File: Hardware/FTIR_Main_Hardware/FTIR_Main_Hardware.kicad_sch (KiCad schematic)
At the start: 62 parts, among them J1 RJ45_LED_Shielded, Q1 IRF7606PBF, Q2 BSS138, Q3 IRF7606PBF, Q4 IRF7606PBF, Q5 BSS138, Q6 BSS138, U1 MCP6L01x-xOT, U3 OKI, U5 MCP6L01x-xOT, U6 Teensy4.1_DEV-16771, U7 OKI

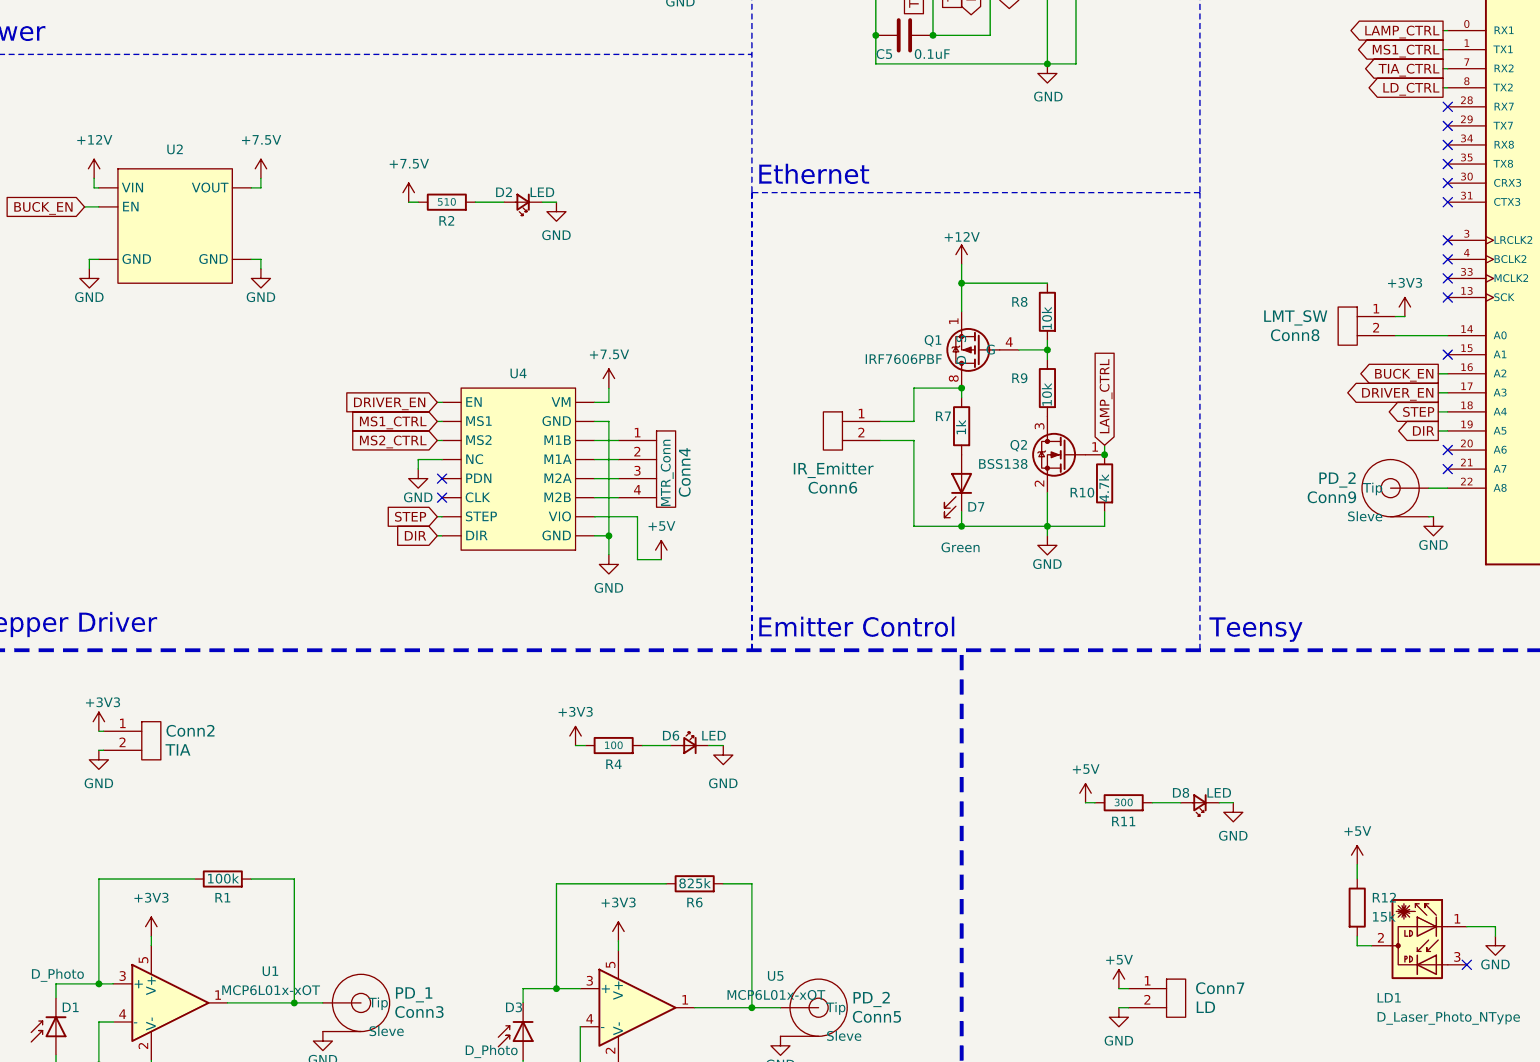
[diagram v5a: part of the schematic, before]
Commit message: Footprint assignments
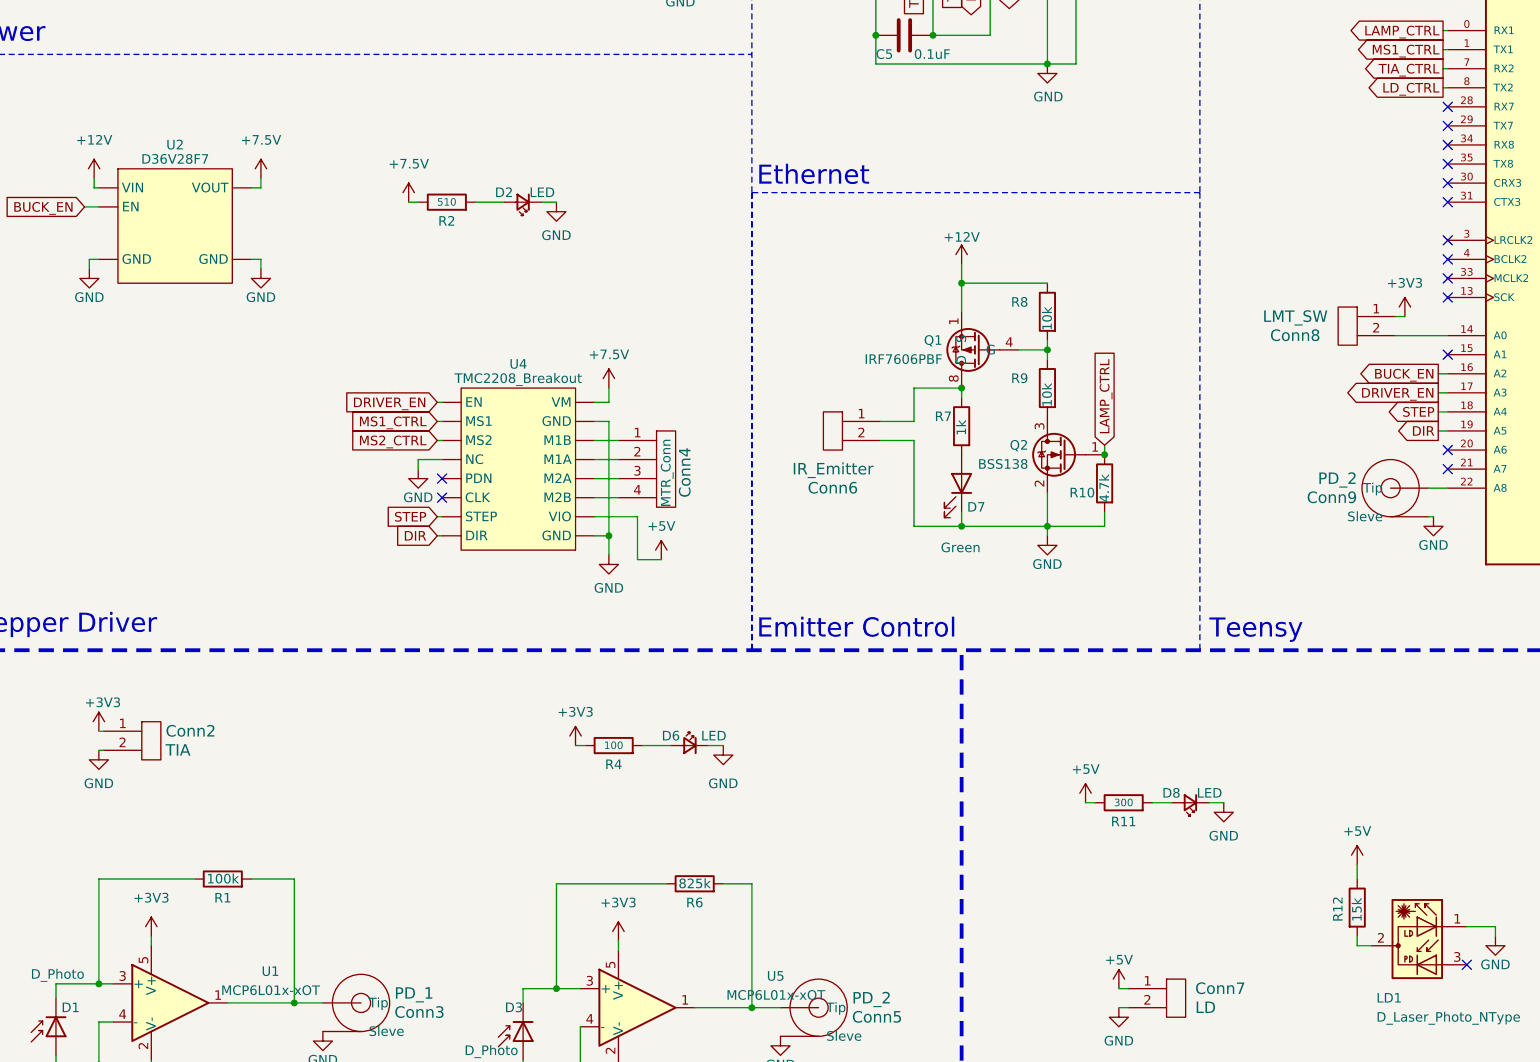
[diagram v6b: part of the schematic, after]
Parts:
- Conn1: footprint (none) -> MRDT_Connectors:Anderson_2_Horizontal_Stacked
- Conn11, Conn12, Conn2, Conn6, Conn7, Conn8: footprint (none) -> MRDT_Connectors:MOLEX_SL_02_Vertical
- Conn4: footprint (none) -> MRDT_Connectors:MOLEX_SL_04_Vertical
- R1, R12, R6: footprint (none) -> LED_SMD:LED_0603_1608Metric_Pad1.05x0.95mm_HandSolder
- U2: value ~ -> D36V28F7
- U3, U7: footprint (none) -> MRDT_Devices:OKI_Horizontal
- U4: value ~ -> TMC2208_Breakout
- U6: footprint MODULE_DEV-16771 -> MRDT_Shields:Teensy_4_1
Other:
- moved on the sheet: D8
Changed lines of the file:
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@@
     (stroke (width 0) (type default))
   )
-  (wire (pts (xy 179.705 154.305) (xy 181.61 154.305))
+  (wire (pts (xy 178.435 154.305) (xy 180.34 154.305))
     (stroke (width 0) (type default))
   )
@@
     (stroke (width 0) (type default))
   )
-  (wire (pts (xy 170.815 154.305) (xy 174.625 154.305))
+  (wire (pts (xy 170.815 154.305) (xy 173.355 154.305))
     (stroke (width 0) (type default))
   )
@@
     )
   )
-  (symbol (lib_id "Device:LED_Small") (at 177.165 154.305 180) (unit 1)
+  (symbol (lib_id "Device:LED_Small") (at 175.895 154.305 180) (unit 1)
     (in_bom yes) (on_board yes) (dnp no)
-    (property "Reference" "D8" (at 174.625 153.035 0)
+    (property "Reference" "D8" (at 173.355 153.035 0)
       (effects (font (size 1.27 1.27)))
     )
-    (property "Value" "LED" (at 179.705 153.035 0)
+    (property "Value" "LED" (at 178.435 153.035 0)
       (effects (font (size 1.27 1.27)))
     )
-    (property "Footprint" "LED_SMD:LED_0603_1608Metric_Pad1.05x0.95mm_HandSolder" (at 177.165 154.305 90)
+    (property "Footprint" "LED_SMD:LED_0603_1608Metric_Pad1.05x0.95mm_HandSolder" (at 175.895 154.305 90)
       (effects (font (size 1.27 1.27)) hide)
     )
-    (property "Datasheet" "~" (at 177.165 154.305 90)
+    (property "Datasheet" "~" (at 175.895 154.305 90)
       (effects (font (size 1.27 1.27)) hide)
     )
@@
   )
   (symbol (lib_name "Pololu_7v5_Stepdown_1") (lib_id "Stepper_Driver_Headers:Pololu_7v5_Stepdown") (at 40.64 75.565 0) (unit 1)
-    (in_bom yes) (on_board yes) (dnp no) (fields_autoplaced)
-    (property "Reference" "U2" (at 40.64 67.31 0)
+    (in_bom yes) (on_board yes) (dnp no)
+    (property "Reference" "U2" (at 40.64 66.675 0)
       (effects (font (size 1.27 1.27)))
     )
-    (property "Value" "~" (at 40.64 75.565 0)
+    (property "Value" "D36V28F7" (at 40.64 68.58 0)
       (effects (font (size 1.27 1.27)))
     )
@@
       (effects (font (size 1.524 1.524)))
     )
-    (property "Footprint" "" (at 322.58 93.345 0)
+    (property "Footprint" "MRDT_Connectors:MOLEX_SL_02_Vertical" (at 322.58 93.345 0)
       (effects (font (size 1.524 1.524)) hide)
     )
@@
   (symbol (lib_id "Stepper_Driver_Headers:TMC2208_Breakout") (at 86.36 115.57 180) (unit 1)
     (in_bom yes) (on_board yes) (dnp no)
-    (property "Reference" "U4" (at 86.36 97.155 0)
+    (property "Reference" "U4" (at 86.36 95.885 0)
       (effects (font (size 1.27 1.27)))
     )
-    (property "Value" "~" (at 87.63 115.57 0)
+    (property "Value" "TMC2208_Breakout" (at 86.36 97.79 0)
       (effects (font (size 1.27 1.27)))
     )
@@
   (symbol (lib_id "Device:R") (at 198.12 168.275 0) (unit 1)
     (in_bom yes) (on_board yes) (dnp no)
-    (property "Reference" "R12" (at 200.025 167.005 0)
+    (property "Reference" "R12" (at 195.58 170.18 90)
       (effects (font (size 1.27 1.27)) (justify left))
     )
-    (property "Value" "15k" (at 200.025 169.545 0)
+    (property "Value" "15k" (at 198.12 170.18 90)
       (effects (font (size 1.27 1.27)) (justify left))
     )
-    (property "Footprint" "" (at 196.342 168.275 90)
+    (property "Footprint" "LED_SMD:LED_0603_1608Metric_Pad1.05x0.95mm_HandSolder" (at 196.342 168.275 90)
       (effects (font (size 1.27 1.27)) hide)
     )
@@
       (effects (font (size 1.524 1.524)))
     )
-    (property "Footprint" "" (at 198.12 95.885 0)
+    (property "Footprint" "MRDT_Connectors:MOLEX_SL_02_Vertical" (at 198.12 95.885 0)
       (effects (font (size 1.524 1.524)) hide)
     )
@@
       (effects (font (size 1.524 1.524)) (justify left))
     )
-    (property "Footprint" "" (at 36.195 151.13 0)
+    (property "Footprint" "MRDT_Connectors:MOLEX_SL_02_Vertical" (at 36.195 151.13 0)
       (effects (font (size 1.524 1.524)) hide)
     )
@@
       (effects (font (size 1.27 1.27)))
     )
-    (property "Footprint" "" (at 109.855 166.878 90)
+    (property "Footprint" "LED_SMD:LED_0603_1608Metric_Pad1.05x0.95mm_HandSolder" (at 109.855 166.878 90)
       (effects (font (size 1.27 1.27)) hide)
     )
@@
     )
   )
-  (symbol (lib_id "power:GND") (at 181.61 154.305 0) (unit 1)
+  (symbol (lib_id "power:GND") (at 180.34 154.305 0) (unit 1)
     (in_bom yes) (on_board yes) (dnp no) (fields_autoplaced)
-    (property "Reference" "#PWR033" (at 181.61 160.655 0)
+    (property "Reference" "#PWR033" (at 180.34 160.655 0)
       (effects (font (size 1.27 1.27)) hide)
     )
-    (property "Value" "GND" (at 181.61 158.75 0)
+    (property "Value" "GND" (at 180.34 158.75 0)
       (effects (font (size 1.27 1.27)))
     )
-    (property "Footprint" "" (at 181.61 154.305 0)
+    (property "Footprint" "" (at 180.34 154.305 0)
       (effects (font (size 1.27 1.27)) hide)
     )
-    (property "Datasheet" "" (at 181.61 154.305 0)
+    (property "Datasheet" "" (at 180.34 154.305 0)
       (effects (font (size 1.27 1.27)) hide)
     )
@@
       (effects (font (size 1.27 1.27)) (justify left))
     )
-    (property "Footprint" "" (at 104.775 114.935 0)
+    (property "Footprint" "MRDT_Connectors:MOLEX_SL_04_Vertical" (at 104.775 114.935 0)
       (effects (font (size 1.524 1.524)) hide)
     )
@@
       (effects (font (size 1.524 1.524)))
     )
-    (property "Footprint" "" (at 304.165 116.84 0)
+    (property "Footprint" "MRDT_Devices:OKI_Horizontal" (at 304.165 116.84 0)
       (effects (font (size 1.524 1.524)) hide)
     )
@@
       (effects (font (size 1.524 1.524)) (justify left))
     )
-    (property "Footprint" "" (at 172.72 185.42 0)
+    (property "Footprint" "MRDT_Connectors:MOLEX_SL_02_Vertical" (at 172.72 185.42 0)
       (effects (font (size 1.524 1.524)) hide)
     )
@@
       (effects (font (size 1.524 1.524)))
     )
-    (property "Footprint" "" (at 49.53 33.655 0)
+    (property "Footprint" "MRDT_Devices:OKI_Horizontal" (at 49.53 33.655 0)
       (effects (font (size 1.524 1.524)) hide)
     )
@@
       (effects (font (size 1.27 1.27)))
     )
-    (property "Footprint" "MODULE_DEV-16771" (at 283.845 79.375 0)
+    (property "Footprint" "MRDT_Shields:Teensy_4_1" (at 283.845 79.375 0)
       (effects (font (size 1.27 1.27)) (justify left bottom) hide)
     )
@@
       (effects (font (size 1.524 1.524)))
     )
-    (property "Footprint" "" (at 27.94 55.245 0)
+    (property "Footprint" "MRDT_Connectors:Anderson_2_Horizontal_Stacked" (at 27.94 55.245 0)
       (effects (font (size 1.524 1.524)) hide)
     )
@@
       (effects (font (size 1.524 1.524)))
     )
-    (property "Footprint" "" (at 321.31 49.53 0)
+    (property "Footprint" "MRDT_Connectors:MOLEX_SL_02_Vertical" (at 321.31 49.53 0)
       (effects (font (size 1.524 1.524)) hide)
     )
@@
       (effects (font (size 1.27 1.27)))
     )
-    (property "Footprint" "" (at 46.99 166.243 90)
+    (property "Footprint" "LED_SMD:LED_0603_1608Metric_Pad1.05x0.95mm_HandSolder" (at 46.99 166.243 90)
       (effects (font (size 1.27 1.27)) hide)
     )
@@
       (effects (font (size 1.524 1.524)))
     )
-    (property "Footprint" "" (at 129.54 109.855 0)
+    (property "Footprint" "MRDT_Connectors:MOLEX_SL_02_Vertical" (at 129.54 109.855 0)
       (effects (font (size 1.524 1.524)) hide)
     )
@@
       (effects (font (size 1.524 1.524)))
     )
-    (property "Footprint" "" (at 27.94 45.085 0)
+    (property "Footprint" "MRDT_Connectors:Anderson_2_Horizontal_Stacked" (at 27.94 45.085 0)
       (effects (font (size 1.524 1.524)) hide)
     )

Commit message: Minor Changes
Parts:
- R1: value 100k -> ~
- R6: value 825k -> ~
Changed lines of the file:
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@@
   (symbol (lib_id "Device:R") (at 109.855 165.1 90) (unit 1)
     (in_bom yes) (on_board yes) (dnp no)
-    (property "Reference" "R6" (at 109.855 167.64 90)
-      (effects (font (size 1.27 1.27)))
-    )
-    (property "Value" "825k" (at 109.855 165.1 90)
+    (property "Reference" "R6" (at 109.855 165.1 90)
+      (effects (font (size 1.27 1.27)))
+    )
+    (property "Value" "~" (at 109.855 165.1 90)
       (effects (font (size 1.27 1.27)))
     )
@@
       (effects (font (size 1.27 1.27)) hide)
     )
-    (property "Value" "+3V3" (at 37.465 167.005 0)
+    (property "Value" "+3V3" (at 37.465 168.275 0)
       (effects (font (size 1.27 1.27)))
     )
@@
   (symbol (lib_id "Device:R") (at 46.99 164.465 90) (unit 1)
     (in_bom yes) (on_board yes) (dnp no)
-    (property "Reference" "R1" (at 46.99 167.005 90)
-      (effects (font (size 1.27 1.27)))
-    )
-    (property "Value" "100k" (at 46.99 164.465 90)
+    (property "Reference" "R1" (at 46.99 164.465 90)
+      (effects (font (size 1.27 1.27)))
+    )
+    (property "Value" "~" (at 46.99 164.465 90)
       (effects (font (size 1.27 1.27)))
     )
@@
       (effects (font (size 1.27 1.27)) hide)
     )
-    (property "Value" "+3V3" (at 99.695 167.64 0)
-      (effects (font (size 1.27 1.27)))
-    )
+    (property "Value" "+3V3" (at 99.695 168.91 0)
+      (effects (font (size 1.27 1.27)))
+    )

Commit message: Review pt.2 changes
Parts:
- added R1, R5: ~, LED_SMD:LED_0603_1608Metric_Pad1.05x0.95mm_HandSolder, symbol Device:R
- D2, D4, D5, D6, D8: value LED -> Green
- R14: renamed from R12; value 15k -> 85
- R17: renamed from R15; value 5.1k -> 3.3k
- renumbered C3 to C2, C5 to C3, C6 to C4, C7 to C5, R8 to R10, R9 to R11, R10 to R12, R11 to R13, R13 to R15, R14 to R16, R16 to R18, R17 to R19, R1 to R2, R18 to R20, R19 to R21, R20 to R22, R2 to R3, R3 to R4, R4 to R6, R5 to R7, R6 to R8, R7 to R9
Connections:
- net +3V3: now also U1.2 (V-), U4. (VM); no longer U1.5 (V+)
- net +5V: no longer U4. (VM)
- net GND: now also U1.3 (+), U1.5 (V+); no longer U1.2 (V-), U1.4 (-)
- net at D3.1 (K), U5.3 (+): now also R5.1; no longer R8.1
- new net: D1.1 (K), R1.1, U1.4 (-)
- new net: R5.2, R8.1
- new net: R1.2, R2.1
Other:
- moved on the sheet: C3, D10, D9, R17, R18
